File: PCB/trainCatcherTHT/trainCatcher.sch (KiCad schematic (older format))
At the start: 35 parts, among them J1 Power, J2 break, J3 Conn_01x04_Male, J4 thru, J5 thru, Q1 IRF540N, Q2 IRF540N, U1 MC78L05_TO92, U2 ATtiny13-20PU, U3 SFH617A-1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

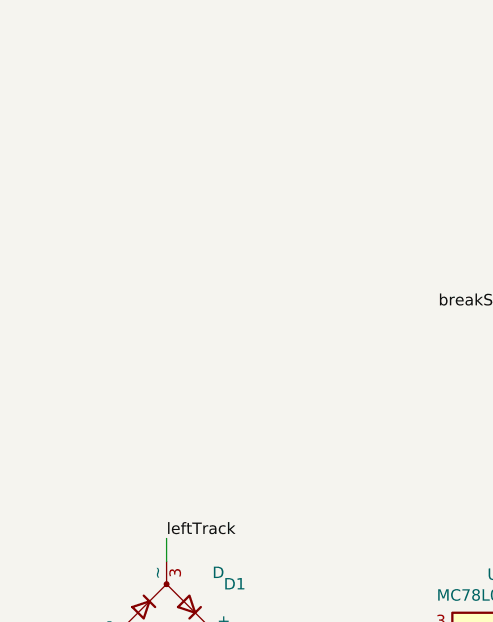
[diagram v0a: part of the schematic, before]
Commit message: changed PCB design of tht trainCatcher
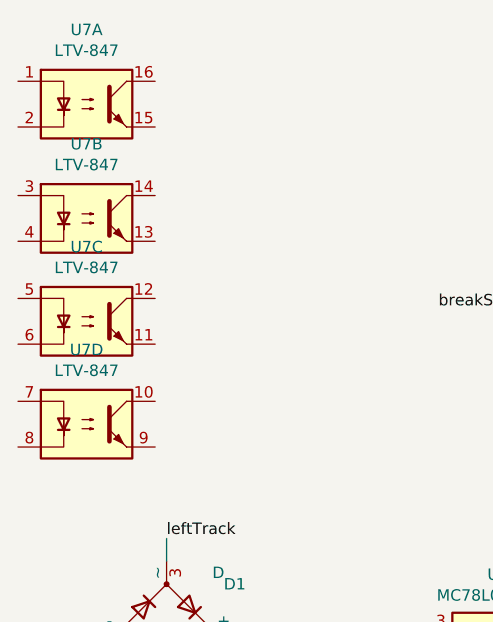
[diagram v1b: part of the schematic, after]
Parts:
- added U7: LTV-847, Package_DIP:DIP-16_W7.62mm, symbol Isolator:LTV-847
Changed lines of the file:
@@
 Wire Wire Line
 	7400 3700 7400 4250
+$Comp
+L Isolator:LTV-847 U7
+U 1 1 62045CE4
+P 1250 850
+F 0 "U7" H 1250 1175 50  0000 C CNN
+F 1 "LTV-847" H 1250 1084 50  0000 C CNN
+F 2 "Package_DIP:DIP-16_W7.62mm" H 1050 650 50  0001 L CIN
+F 3 "http://optoelectronics.liteon.com/upload/download/DS-70-96-0016/LTV-8X7%20series.PDF" H 1250 850 50  0001 L CNN
+	1    1250 850
+	1    0    0    -1
+$EndComp
+$Comp
+L Isolator:LTV-847 U7
+U 2 1 62047560
+P 1250 1350
+F 0 "U7" H 1250 1675 50  0000 C CNN
+F 1 "LTV-847" H 1250 1584 50  0000 C CNN
+F 2 "Package_DIP:DIP-16_W7.62mm" H 1050 1150 50  0001 L CIN
+F 3 "http://optoelectronics.liteon.com/upload/download/DS-70-96-0016/LTV-8X7%20series.PDF" H 1250 1350 50  0001 L CNN
+	2    1250 1350
+	1    0    0    -1
+$EndComp
+$Comp
+L Isolator:LTV-847 U7
+U 3 1 62048522
+P 1250 1800
+F 0 "U7" H 1250 2125 50  0000 C CNN
+F 1 "LTV-847" H 1250 2034 50  0000 C CNN
+F 2 "Package_DIP:DIP-16_W7.62mm" H 1050 1600 50  0001 L CIN
+F 3 "http://optoelectronics.liteon.com/upload/download/DS-70-96-0016/LTV-8X7%20series.PDF" H 1250 1800 50  0001 L CNN
+	3    1250 1800
+	1    0    0    -1
+$EndComp
+$Comp
+L Isolator:LTV-847 U7
+U 4 1 6204A478
+P 1250 2250
+F 0 "U7" H 1250 2575 50  0000 C CNN
+F 1 "LTV-847" H 1250 2484 50  0000 C CNN
+F 2 "Package_DIP:DIP-16_W7.62mm" H 1050 2050 50  0001 L CIN
+F 3 "http://optoelectronics.liteon.com/upload/download/DS-70-96-0016/LTV-8X7%20series.PDF" H 1250 2250 50  0001 L CNN
+	4    1250 2250
+	1    0    0    -1
+$EndComp
 $EndSCHEMATC

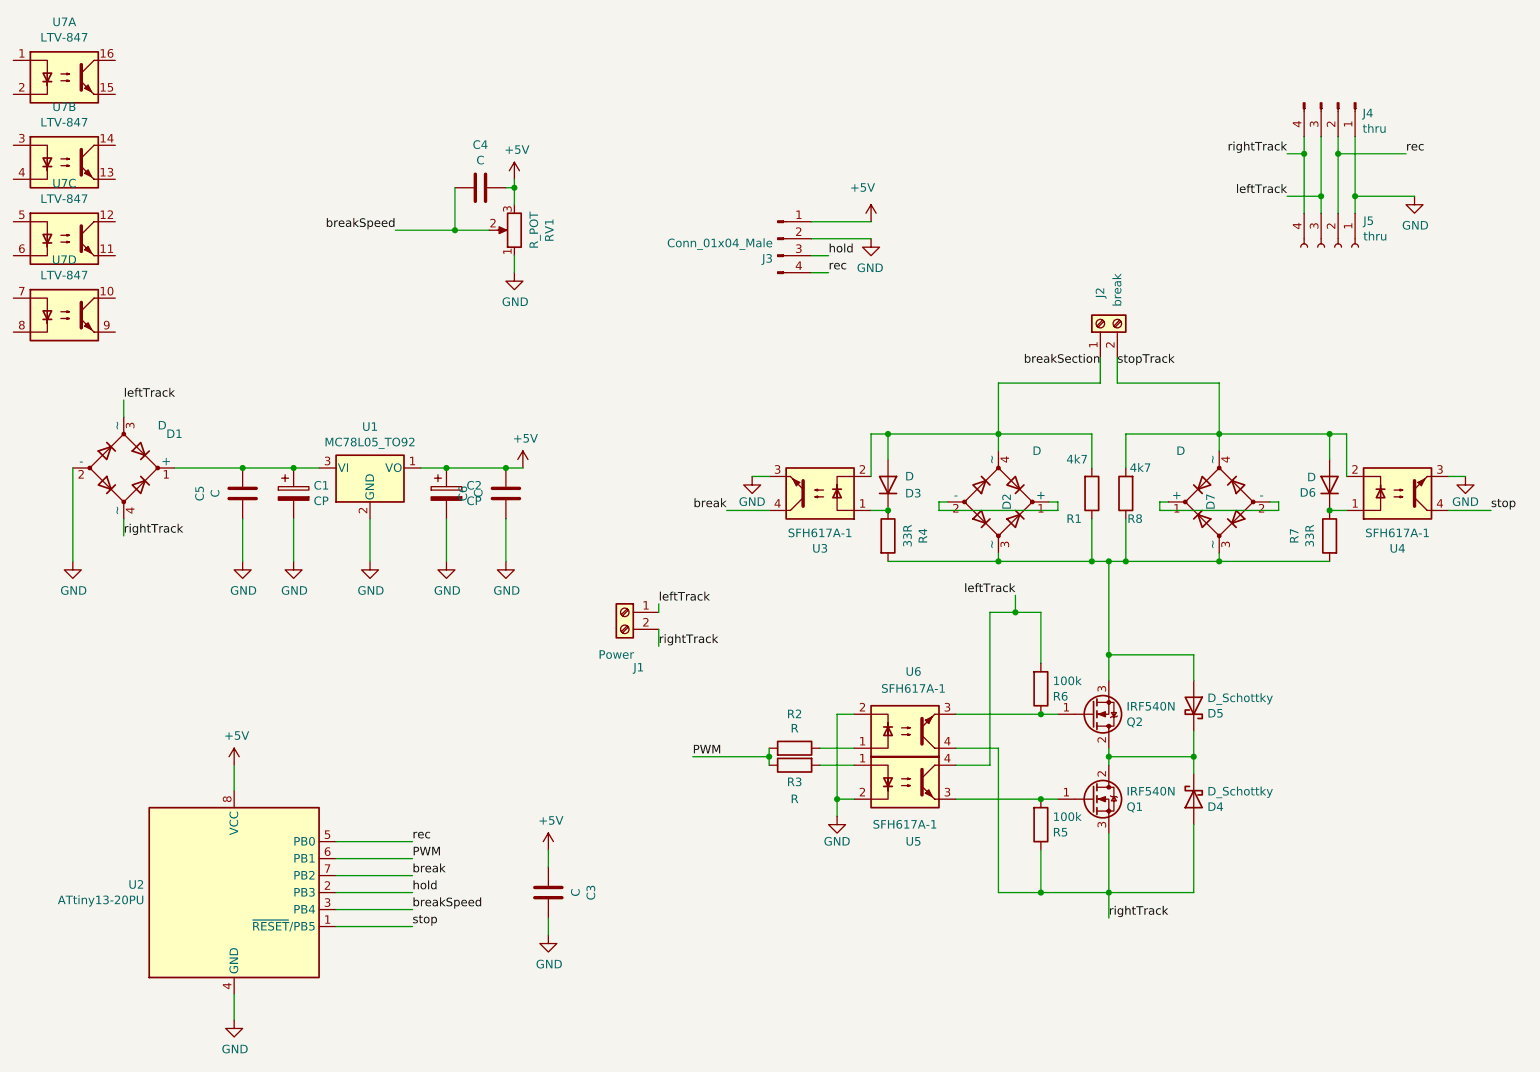
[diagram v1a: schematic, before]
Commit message: changed pulse time from 1ms to 500us
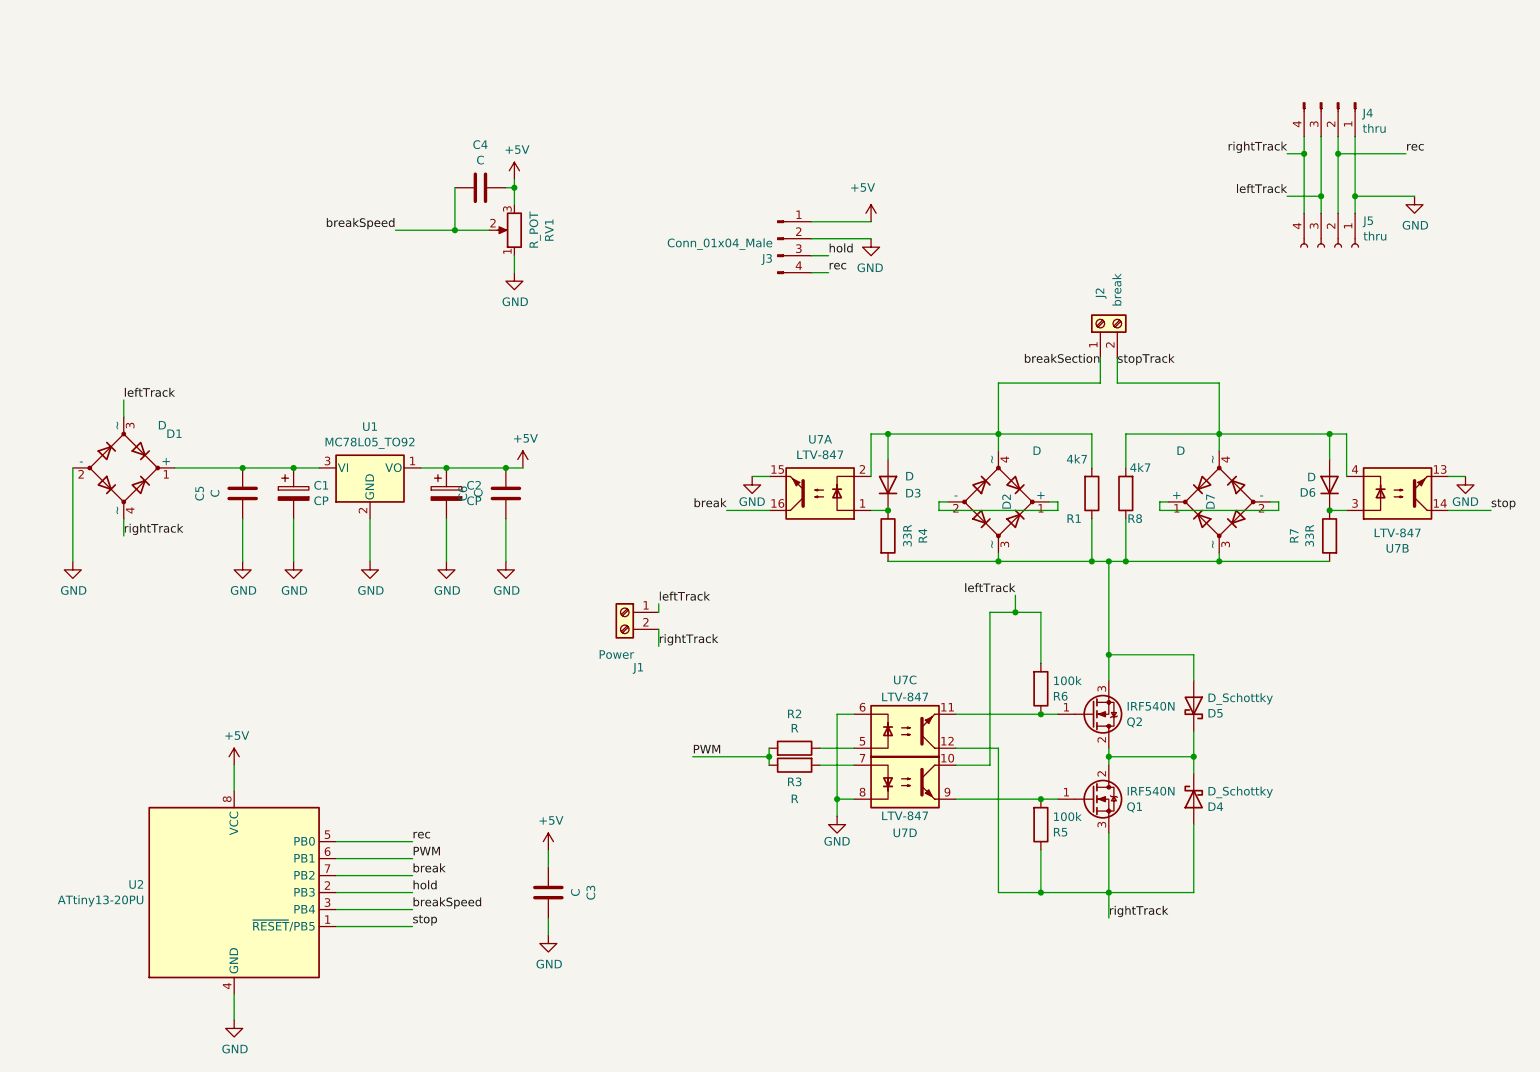
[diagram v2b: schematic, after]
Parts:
- removed U3, U4, U5, U6: SFH617A-1, Package_DIP:DIP-4_W7.62mm, symbol Isolator:SFH617A-1
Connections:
- net GND: now also U7.13, U7.15, U7.6, U7.8
- net break: now also U7.16
- net breakSection: now also U7.2
- net leftTrack: now also U7.10
- net rightTrack: now also U7.12
- net stop: now also U7.14
- net stopTrack: now also U7.4
- net at R2.1: now also U7.5
- net at R3.2: now also U7.7
- net at D3.1 (K), R4.1: now also U7.1
- net at Q2.1 (G), R6.1: now also U7.11
- net at Q1.1 (G), R5.2: now also U7.9
- net at D6.1 (K), R7.1: now also U7.3
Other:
- moved on the sheet: U7A, U7B, U7C, U7D
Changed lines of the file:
@@
 Wire Wire Line
 	2300 3450 2300 3700
-$Comp
-L Isolator:SFH617A-1 U5
-U 1 1 61E0D8F1
-P 6200 5000
-F 0 "U5" H 6250 4650 50  0000 C CNN
-F 1 "SFH617A-1" H 6200 4750 50  0000 C CNN
-F 2 "Package_DIP:DIP-4_W7.62mm" H 6000 4800 50  0001 L CIN
-F 3 "http://www.vishay.com/docs/83740/sfh617a.pdf" H 6200 5000 50  0001 L CNN
-	1    6200 5000
-	1    0    0    -1
-$EndComp
 Wire Wire Line
 	6750 5650 6750 4800
@@
 Wire Wire Line
 	4950 4850 5400 4850
-$Comp
-L Isolator:SFH617A-1 U6
-U 1 1 61E0BF7C
-P 6200 4700
-F 0 "U6" H 6250 4350 50  0000 C CNN
-F 1 "SFH617A-1" H 6250 4450 50  0000 C CNN
-F 2 "Package_DIP:DIP-4_W7.62mm" H 6000 4500 50  0001 L CIN
-F 3 "http://www.vishay.com/docs/83740/sfh617a.pdf" H 6200 4700 50  0001 L CNN
-	1    6200 4700
-	1    0    0    1
-$EndComp
 Wire Wire Line
 	5900 4800 5700 4800
@@
 Wire Wire Line
 	6750 3700 6100 3700
-$Comp
-L Isolator:SFH617A-1 U3
-U 1 1 61E04D4A
-P 5700 3300
-F 0 "U3" H 5700 3625 50  0000 C CNN
-F 1 "SFH617A-1" H 5700 3534 50  0000 C CNN
-F 2 "Package_DIP:DIP-4_W7.62mm" H 5500 3100 50  0001 L CIN
-F 3 "http://www.vishay.com/docs/83740/sfh617a.pdf" H 5700 3300 50  0001 L CNN
-	1    5700 3300
-	-1   0    0    1
-$EndComp
 Text Label 7450 2550 0    50   ~ 0
 stopTrack
@@
 Wire Wire Line
 	8050 3700 8700 3700
-$Comp
-L Isolator:SFH617A-1 U4
-U 1 1 61E0B7C3
-P 9100 3300
-F 0 "U4" H 9100 3625 50  0000 C CNN
-F 1 "SFH617A-1" H 9100 3534 50  0000 C CNN
-F 2 "Package_DIP:DIP-4_W7.62mm" H 8900 3100 50  0001 L CIN
-F 3 "http://www.vishay.com/docs/83740/sfh617a.pdf" H 9100 3300 50  0001 L CNN
-	1    9100 3300
-	1    0    0    1
-$EndComp
 Connection ~ 8050 2950
 Wire Wire Line
@@
 L Isolator:LTV-847 U7
 U 1 1 62045CE4
-P 1250 850
-F 0 "U7" H 1250 1175 50  0000 C CNN
-F 1 "LTV-847" H 1250 1084 50  0000 C CNN
-F 2 "Package_DIP:DIP-16_W7.62mm" H 1050 650 50  0001 L CIN
-F 3 "http://optoelectronics.liteon.com/upload/download/DS-70-96-0016/LTV-8X7%20series.PDF" H 1250 850 50  0001 L CNN
-	1    1250 850
-	1    0    0    -1
+P 5700 3300
+F 0 "U7" H 5700 2983 50  0000 C CNN
+F 1 "LTV-847" H 5700 3074 50  0000 C CNN
+F 2 "Package_DIP:DIP-16_W7.62mm" H 5500 3100 50  0001 L CIN
+F 3 "http://optoelectronics.liteon.com/upload/download/DS-70-96-0016/LTV-8X7%20series.PDF" H 5700 3300 50  0001 L CNN
+	1    5700 3300
+	-1   0    0    1
 $EndComp
 $Comp
 L Isolator:LTV-847 U7
 U 2 1 62047560
-P 1250 1350
-F 0 "U7" H 1250 1675 50  0000 C CNN
-F 1 "LTV-847" H 1250 1584 50  0000 C CNN
-F 2 "Package_DIP:DIP-16_W7.62mm" H 1050 1150 50  0001 L CIN
-F 3 "http://optoelectronics.liteon.com/upload/download/DS-70-96-0016/LTV-8X7%20series.PDF" H 1250 1350 50  0001 L CNN
-	2    1250 1350
-	1    0    0    -1
+P 9100 3300
+F 0 "U7" H 9100 3625 50  0000 C CNN
+F 1 "LTV-847" H 9100 3534 50  0000 C CNN
+F 2 "Package_DIP:DIP-16_W7.62mm" H 8900 3100 50  0001 L CIN
+F 3 "http://optoelectronics.liteon.com/upload/download/DS-70-96-0016/LTV-8X7%20series.PDF" H 9100 3300 50  0001 L CNN
+	2    9100 3300
+	1    0    0    1
 $EndComp
 $Comp
 L Isolator:LTV-847 U7
 U 3 1 62048522
-P 1250 1800
-F 0 "U7" H 1250 2125 50  0000 C CNN
-F 1 "LTV-847" H 1250 2034 50  0000 C CNN
-F 2 "Package_DIP:DIP-16_W7.62mm" H 1050 1600 50  0001 L CIN
-F 3 "http://optoelectronics.liteon.com/upload/download/DS-70-96-0016/LTV-8X7%20series.PDF" H 1250 1800 50  0001 L CNN
-	3    1250 1800
-	1    0    0    -1
+P 6200 4700
+F 0 "U7" H 6200 4400 50  0000 C CNN
+F 1 "LTV-847" H 6200 4500 50  0000 C CNN
+F 2 "Package_DIP:DIP-16_W7.62mm" H 6000 4500 50  0001 L CIN
+F 3 "http://optoelectronics.liteon.com/upload/download/DS-70-96-0016/LTV-8X7%20series.PDF" H 6200 4700 50  0001 L CNN
+	3    6200 4700
+	1    0    0    1
 $EndComp
 $Comp
 L Isolator:LTV-847 U7
 U 4 1 6204A478
-P 1250 2250
-F 0 "U7" H 1250 2575 50  0000 C CNN
-F 1 "LTV-847" H 1250 2484 50  0000 C CNN
-F 2 "Package_DIP:DIP-16_W7.62mm" H 1050 2050 50  0001 L CIN
-F 3 "http://optoelectronics.liteon.com/upload/download/DS-70-96-0016/LTV-8X7%20series.PDF" H 1250 2250 50  0001 L CNN
-	4    1250 2250
-	1    0    0    -1
-$EndComp
+P 6200 5000
+F 0 "U7" H 6200 4700 50  0000 C CNN
+F 1 "LTV-847" H 6200 4800 50  0000 C CNN
+F 2 "Package_DIP:DIP-16_W7.62mm" H 6000 4800 50  0001 L CIN
+F 3 "http://optoelectronics.liteon.com/upload/download/DS-70-96-0016/LTV-8X7%20series.PDF" H 6200 5000 50  0001 L CNN
+	4    6200 5000
+	1    0    0    -1
+$EndComp
